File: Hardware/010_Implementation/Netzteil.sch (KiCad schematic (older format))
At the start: 6 parts, among them J1 USB_B_Mini, K1 G2R2A, U1 LT1086-3.3, U2 LM1085-3.3

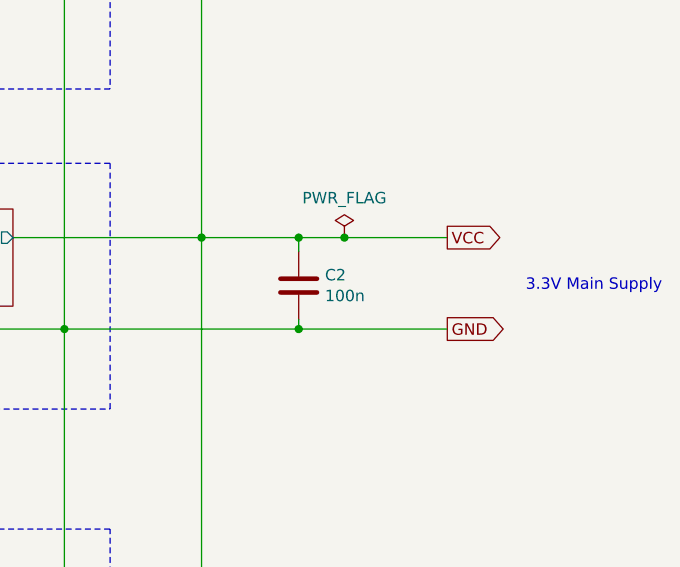
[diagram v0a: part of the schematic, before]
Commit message: Changes to Schematic. Button, LEDs and Power Flags
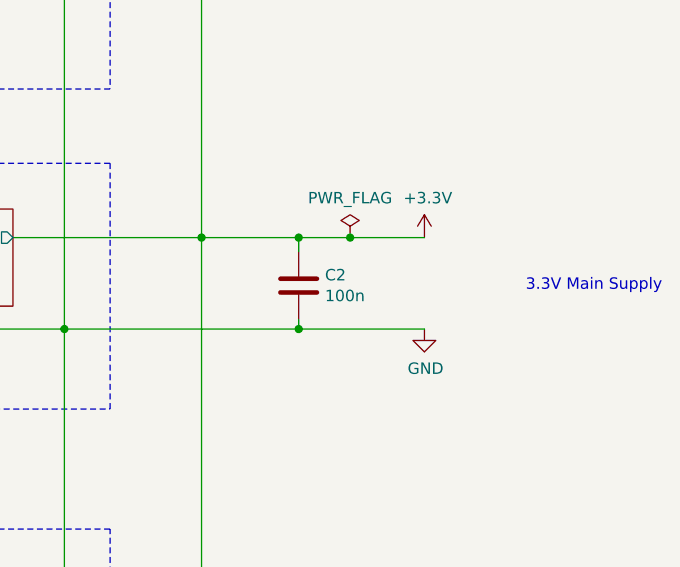
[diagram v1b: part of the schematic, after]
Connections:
- net labels added: +3.3V
- net labels removed: VCC
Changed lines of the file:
@@
 	4125 1850 3725 1850
 Connection ~ 4125 1850
-Text GLabel 9550 3450 2    50   Output ~ 0
-VCC
 Wire Wire Line
 	5725 2150 5725 2250
@@
 	8075 4725 3200 4725
 Connection ~ 6200 3450
-Text GLabel 9550 3850 2    50   Output ~ 0
-GND
 Wire Wire Line
 	8475 5325 8475 3450
@@
 F6 "V_OUT" O R 7600 5325 50
 $EndSheet
-$Comp
-L power:PWR_FLAG #FLG02
-U 1 1 5F5B0BF0
-P 9100 3450
-F 0 "#FLG02" H 9100 3525 50  0001 C CNN
-F 1 "PWR_FLAG" H 9100 3623 50  0000 C CNN
-F 2 "" H 9100 3450 50  0001 C CNN
-F 3 "~" H 9100 3450 50  0001 C CNN
-	1    9100 3450
-	1    0    0    -1
-$EndComp
-Connection ~ 9100 3450
-Wire Wire Line
-	9100 3450 9550 3450
 Wire Wire Line
 	7875 3850 8900 3850
@@
 Connection ~ 8900 3450
 Wire Wire Line
-	8900 3450 9100 3450
-Wire Wire Line
 	8900 3810 8900 3850
 Connection ~ 8900 3850
 Wire Wire Line
-	8900 3850 9550 3850
+	8900 3850 9450 3850
 Text Notes 10490 3690 2    50   ~ 0
 3.3V Main Supply
@@
 	1    0    0    -1
 $EndComp
+$Comp
+L power:GND #PWR02
+U 1 1 5F7C816E
+P 9450 3850
+F 0 "#PWR02" H 9450 3600 50  0001 C CNN
+F 1 "GND" H 9455 3677 50  0000 C CNN
+F 2 "" H 9450 3850 50  0001 C CNN
+F 3 "" H 9450 3850 50  0001 C CNN
+	1    9450 3850
+	1    0    0    -1
+$EndComp
+Wire Wire Line
+	8900 3450 9125 3450
+$Comp
+L power:+3.3V #PWR01
+U 1 1 5F7FF608
+P 9450 3450
+F 0 "#PWR01" H 9450 3300 50  0001 C CNN
+F 1 "+3.3V" H 9465 3623 50  0000 C CNN
+F 2 "" H 9450 3450 50  0001 C CNN
+F 3 "" H 9450 3450 50  0001 C CNN
+	1    9450 3450
+	1    0    0    -1
+$EndComp
+$Comp
+L power:PWR_FLAG #FLG0101
+U 1 1 5F8BED6A
+P 9125 3450
+F 0 "#FLG0101" H 9125 3525 50  0001 C CNN
+F 1 "PWR_FLAG" H 9125 3623 50  0000 C CNN
+F 2 "" H 9125 3450 50  0001 C CNN
+F 3 "~" H 9125 3450 50  0001 C CNN
+	1    9125 3450
+	1    0    0    -1
+$EndComp
+Connection ~ 9125 3450
+Wire Wire Line
+	9125 3450 9450 3450
 $EndSCHEMATC

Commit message: Updated Schematic. Fixed Connection to Ground to prevent Software Bugs
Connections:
- wire segments 54 -> 55
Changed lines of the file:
@@
 L power:PWR_FLAG #FLG01
 U 1 1 5F6C2967
-P 5250 1850
-F 0 "#FLG01" H 5250 1925 50  0001 C CNN
-F 1 "PWR_FLAG" H 5250 2023 50  0000 C CNN
-F 2 "" H 5250 1850 50  0001 C CNN
-F 3 "~" H 5250 1850 50  0001 C CNN
-	1    5250 1850
+P 5250 1775
+F 0 "#FLG01" H 5250 1850 50  0001 C CNN
+F 1 "PWR_FLAG" H 5250 1948 50  0000 C CNN
+F 2 "" H 5250 1775 50  0001 C CNN
+F 3 "~" H 5250 1775 50  0001 C CNN
+	1    5250 1775
 	1    0    0    -1
 $EndComp
@@
 Wire Wire Line
 	9125 3450 9450 3450
+Wire Wire Line
+	5250 1850 5250 1775
 $EndSCHEMATC

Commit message: Modified Board Schematic. Optimized supply and switching system through Software
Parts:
- removed C2: 100n, Capacitor_SMD:C_1812_4532Metric_Pad1.30x3.40mm_HandSolder, symbol Device:C
- removed J1: USB_B_Mini, Connector_USB:USB_Micro-B_Wuerth_629105150521_CircularHoles, symbol Connector:USB_B_Mini
- removed K1: G2R2A, Board:G2R2A, symbol Board:G2R2A
- removed U1: LT1086-3.3, Package_TO_SOT_SMD:TO-263-3_TabPin4, symbol Regulator_Linear:LT1086-3.3
- removed U2: LM1085-3.3, Package_TO_SOT_SMD:TO-263-3_TabPin4, symbol Regulator_Linear:LM1085-3.3
- added C1: 10n, Capacitor_SMD:C_1812_4532Metric_Pad1.30x3.40mm_HandSolder, symbol Device:C
- added R1: 1k, Resistor_SMD:R_0805_2012Metric_Pad1.15x1.40mm_HandSolder, symbol Device:R
- added R2: 100, Resistor_SMD:R_0805_2012Metric_Pad1.15x1.40mm_HandSolder, symbol Device:R
- added U1: LT1086-5.0, Board:DPAK254P1394X457-4N, symbol Regulator_Linear:LT1086-5.0
- renumbered C1 to C2
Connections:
- net labels added: Ext.5V, OBD_Voltage_Check
- net labels removed: +3.3V, EN_CAN, OBD_GND, USB_GND, USB_VDD
- wire segments 55 -> 22
- no-connect marks 4 -> 0
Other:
- note removed: "3.3V - MCU Power Supply"
- note removed: "3.3V Main Supply"
- note removed: "5V - External Power Supply"
- moved on the sheet: C2

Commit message: Added Missing 5V marker
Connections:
- net labels added: +5V
- net labels removed: Ext.5V
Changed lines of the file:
@@
 Wire Wire Line
 	6850 2825 7025 2825
-Text HLabel 7950 2825 2    50   Input ~ 0
-Ext.5V
 $Comp
 L power:GND #PWR02
@@
 Wire Wire Line
 	4850 4150 4650 4150
+$Comp
+L power:+5V #PWR?
+U 1 1 5FA170AE
+P 7950 2825
+F 0 "#PWR?" H 7950 2675 50  0001 C CNN
+F 1 "+5V" H 7965 2998 50  0000 C CNN
+F 2 "" H 7950 2825 50  0001 C CNN
+F 3 "" H 7950 2825 50  0001 C CNN
+	1    7950 2825
+	1    0    0    -1
+$EndComp
 $EndSCHEMATC

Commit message: Board version 4
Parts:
- removed U1: LT1086-5.0, Board:DPAK254P1394X457-4N, symbol Regulator_Linear:LT1086-5.0
- added C3: 22u, Capacitor_SMD:C_0603_1608Metric_Pad1.05x0.95mm_HandSolder, symbol Device:C
- added L1: 2.2u, Capacitor_SMD:C_0603_1608Metric_Pad1.05x0.95mm_HandSolder, symbol Device:L
- added R3: 100k, Resistor_SMD:R_0805_2012Metric_Pad1.15x1.40mm_HandSolder, symbol Device:R
- added U1: TPS62163DGK, Package_SO:VSSOP-8_3.0x3.0mm_P0.65mm, symbol Regulator_Switching:TPS62163DSG
- C1: footprint Capacitor_SMD:C_1812_4532Metric_Pad1.30x3.40mm_HandSolder -> Capacitor_SMD:C_0603_1608Metric_Pad1.05x0.95mm_HandSolder
- C2: value 100n -> 10u; footprint Capacitor_SMD:C_1812_4532Metric_Pad1.30x3.40mm_HandSolder -> Capacitor_SMD:C_0603_1608Metric_Pad1.05x0.95mm_HandSolder
- R1: value 1k -> 10k
- R2: value 100 -> 1k
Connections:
- wire segments 22 -> 44
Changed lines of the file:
@@
 Text Notes 4175 2300 2    50   ~ 0
 12V-OBD Power Supply
-Wire Wire Line
-	6850 2825 6850 2875
-Wire Wire Line
-	6850 3175 6850 3225
-$Comp
-L Device:C C2
-U 1 1 5F6089EB
-P 6850 3025
-F 0 "C2" H 6965 3071 50  0000 L CNN
-F 1 "100n" H 6965 2980 50  0000 L CNN
-F 2 "Capacitor_SMD:C_1812_4532Metric_Pad1.30x3.40mm_HandSolder" H 6888 2875 50  0001 C CNN
-F 3 "~" H 6850 3025 50  0001 C CNN
-	1    6850 3025
-	1    0    0    -1
-$EndComp
-Wire Wire Line
-	6850 2825 7025 2825
-$Comp
-L power:GND #PWR02
-U 1 1 5FA1043A
-P 7950 3300
-F 0 "#PWR02" H 7950 3050 50  0001 C CNN
-F 1 "GND" H 7955 3127 50  0000 C CNN
-F 2 "" H 7950 3300 50  0001 C CNN
-F 3 "" H 7950 3300 50  0001 C CNN
-	1    7950 3300
-	1    0    0    -1
-$EndComp
-Wire Wire Line
-	7950 3225 7950 3300
-Wire Wire Line
-	6850 2825 6775 2825
-Connection ~ 6850 2825
-Wire Wire Line
-	7625 2825 7950 2825
-$Comp
-L Regulator_Linear:LT1086-5.0 U1
-U 1 1 5FA0C017
-P 7325 2825
-F 0 "U1" H 7325 3067 50  0000 C CNN
-F 1 "LT1086-5.0" H 7325 2976 50  0000 C CNN
-F 2 "Board:DPAK254P1394X457-4N" H 7325 3075 50  0001 C CIN
-F 3 "https://www.analog.com/media/en/technical-documentation/data-sheets/1086ffs.pdf" H 7325 2825 50  0001 C CNN
-	1    7325 2825
-	1    0    0    -1
-$EndComp
-Wire Wire Line
-	6850 3225 7325 3225
-Wire Wire Line
-	7325 3125 7325 3225
-Connection ~ 7325 3225
-Wire Wire Line
-	7325 3225 7950 3225
 $Comp
 L Device:R R1
@@
 P 5025 3425
 F 0 "R1" H 5095 3471 50  0000 L CNN
-F 1 "1k" H 5095 3380 50  0000 L CNN
+F 1 "10k" H 5095 3380 50  0000 L CNN
 F 2 "Resistor_SMD:R_0805_2012Metric_Pad1.15x1.40mm_HandSolder" V 4955 3425 50  0001 C CNN
 F 3 "~" H 5025 3425 50  0001 C CNN
@@
 P 5025 3875
 F 0 "R2" H 5095 3921 50  0000 L CNN
-F 1 "100" H 5095 3830 50  0000 L CNN
+F 1 "1k" H 5095 3830 50  0000 L CNN
 F 2 "Resistor_SMD:R_0805_2012Metric_Pad1.15x1.40mm_HandSolder" V 4955 3875 50  0001 C CNN
 F 3 "~" H 5025 3875 50  0001 C CNN
@@
 L power:PWR_FLAG #FLG01
 U 1 1 5FB093DE
-P 6775 2825
-F 0 "#FLG01" H 6775 2900 50  0001 C CNN
-F 1 "PWR_FLAG" H 6775 2998 50  0000 C CNN
-F 2 "" H 6775 2825 50  0001 C CNN
-F 3 "~" H 6775 2825 50  0001 C CNN
-	1    6775 2825
-	1    0    0    -1
-$EndComp
-Connection ~ 6775 2825
-Wire Wire Line
-	6775 2825 5025 2825
+P 5425 2825
+F 0 "#FLG01" H 5425 2900 50  0001 C CNN
+F 1 "PWR_FLAG" H 5425 2998 50  0000 C CNN
+F 2 "" H 5425 2825 50  0001 C CNN
+F 3 "~" H 5425 2825 50  0001 C CNN
+	1    5425 2825
+	1    0    0    -1
+$EndComp
 $Comp
 L Device:C C1
@@
 F 0 "C1" H 4765 3921 50  0000 L CNN
 F 1 "10n" H 4765 3830 50  0000 L CNN
-F 2 "Capacitor_SMD:C_1812_4532Metric_Pad1.30x3.40mm_HandSolder" H 4688 3725 50  0001 C CNN
+F 2 "Capacitor_SMD:C_0603_1608Metric_Pad1.05x0.95mm_HandSolder" H 4688 3725 50  0001 C CNN
 F 3 "~" H 4650 3875 50  0001 C CNN
 	1    4650 3875
@@
 	4850 4150 4650 4150
 $Comp
-L power:+5V #PWR021
+L power:+5V #PWR05
 U 1 1 5FA170AE
-P 7950 2825
-F 0 "#PWR021" H 7950 2675 50  0001 C CNN
-F 1 "+5V" H 7965 2998 50  0000 C CNN
-F 2 "" H 7950 2825 50  0001 C CNN
-F 3 "" H 7950 2825 50  0001 C CNN
-	1    7950 2825
-	1    0    0    -1
-$EndComp
+P 10625 2750
+F 0 "#PWR05" H 10625 2600 50  0001 C CNN
+F 1 "+5V" H 10640 2923 50  0000 C CNN
+F 2 "" H 10625 2750 50  0001 C CNN
+F 3 "" H 10625 2750 50  0001 C CNN
+	1    10625 2750
+	1    0    0    -1
+$EndComp
+Connection ~ 5425 2825
+Wire Wire Line
+	5425 2825 5025 2825
+Wire Wire Line
+	5425 2825 6975 2825
+$Comp
+L Regulator_Switching:TPS62163DSG U1
+U 1 1 5FB37DEF
+P 7975 3125
+F 0 "U1" H 7975 3692 50  0000 C CNN
+F 1 "TPS62163DGK" H 7975 3601 50  0000 C CNN
+F 2 "Package_SO:VSSOP-8_3.0x3.0mm_P0.65mm" H 8125 2775 50  0001 L CNN
+F 3 "http://www.ti.com/lit/ds/symlink/tps62160.pdf" H 7975 3675 50  0001 C CNN
+	1    7975 3125
+	1    0    0    -1
+$EndComp
+$Comp
+L Device:L L1
+U 1 1 5FB3AA0A
+P 8650 2825
+F 0 "L1" V 8840 2825 50  0000 C CNN
+F 1 "2.2u" V 8749 2825 50  0000 C CNN
+F 2 "Capacitor_SMD:C_0603_1608Metric_Pad1.05x0.95mm_HandSolder" H 8650 2825 50  0001 C CNN
+F 3 "~" H 8650 2825 50  0001 C CNN
+	1    8650 2825
+	0    -1   -1   0
+$EndComp
+$Comp
+L Device:R R3
+U 1 1 5FB3B31A
+P 8250 4225
+F 0 "R3" V 8043 4225 50  0000 C CNN
+F 1 "100k" V 8134 4225 50  0000 C CNN
+F 2 "Resistor_SMD:R_0805_2012Metric_Pad1.15x1.40mm_HandSolder" V 8180 4225 50  0001 C CNN
+F 3 "~" H 8250 4225 50  0001 C CNN
+	1    8250 4225
+	0    1    1    0
+$EndComp
+Wire Wire Line
+	8375 2825 8500 2825
+Wire Wire Line
+	8800 2825 8925 2825
+Wire Wire Line
+	7575 3225 7575 4225
+Wire Wire Line
+	7575 4225 8100 4225
+Wire Wire Line
+	8925 4225 8925 2925
+Connection ~ 8925 2825
+Wire Wire Line
+	8400 4225 8925 4225
+$Comp
+L power:GND #PWR03
+U 1 1 5FB3F4B3
+P 7975 3750
+F 0 "#PWR03" H 7975 3500 50  0001 C CNN
+F 1 "GND" H 7980 3577 50  0000 C CNN
+F 2 "" H 7975 3750 50  0001 C CNN
+F 3 "" H 7975 3750 50  0001 C CNN
+	1    7975 3750
+	1    0    0    -1
+$EndComp
+Wire Wire Line
+	7975 3750 7975 3575
+Wire Wire Line
+	8075 3575 8075 3525
+Connection ~ 7975 3575
+Wire Wire Line
+	7975 3575 8075 3575
+Wire Wire Line
+	7975 3525 7975 3575
+Wire Wire Line
+	8375 2925 8925 2925
+Connection ~ 8925 2925
+Wire Wire Line
+	8925 2925 8925 2825
+$Comp
+L Device:C C2
+U 1 1 5FB43F56
+P 6975 3100
+F 0 "C2" H 7090 3146 50  0000 L CNN
+F 1 "10u" H 7090 3055 50  0000 L CNN
+F 2 "Capacitor_SMD:C_0603_1608Metric_Pad1.05x0.95mm_HandSolder" H 7013 2950 50  0001 C CNN
+F 3 "~" H 6975 3100 50  0001 C CNN
+	1    6975 3100
+	1    0    0    -1
+$EndComp
+Wire Wire Line
+	7575 2925 7450 2925
+Wire Wire Line
+	7450 2925 7450 2825
+Connection ~ 7450 2825
+Wire Wire Line
+	7450 2825 7575 2825
+Wire Wire Line
+	6975 2950 6975 2825
+Connection ~ 6975 2825
+Wire Wire Line
+	6975 2825 7450 2825
+$Comp
+L power:GND #PWR02
+U 1 1 5FB459AA
+P 6975 3425
+F 0 "#PWR02" H 6975 3175 50  0001 C CNN
+F 1 "GND" H 6980 3252 50  0000 C CNN
+F 2 "" H 6975 3425 50  0001 C CNN
+F 3 "" H 6975 3425 50  0001 C CNN
+	1    6975 3425
+	1    0    0    -1
+$EndComp
+Wire Wire Line
+	6975 3425 6975 3250
+$Comp
+L power:GND #PWR04
+U 1 1 5FB4620B
+P 9975 3500
+F 0 "#PWR04" H 9975 3250 50  0001 C CNN
+F 1 "GND" H 9980 3327 50  0000 C CNN
+F 2 "" H 9975 3500 50  0001 C CNN
+F 3 "" H 9975 3500 50  0001 C CNN
+	1    9975 3500
+	1    0    0    -1
+$EndComp
+Wire Wire Line
+	10625 2825 10625 2750
+$Comp
+L Device:C C3
+U 1 1 5FB437F9
+P 9975 3025
+F 0 "C3" H 10090 3071 50  0000 L CNN
+F 1 "22u" H 10090 2980 50  0000 L CNN
+F 2 "Capacitor_SMD:C_0603_1608Metric_Pad1.05x0.95mm_HandSolder" H 10013 2875 50  0001 C CNN
+F 3 "~" H 9975 3025 50  0001 C CNN
+	1    9975 3025
+	1    0    0    -1
+$EndComp
+Wire Wire Line
+	8925 2825 9975 2825
+Wire Wire Line
+	9975 2875 9975 2825
+Connection ~ 9975 2825
+Wire Wire Line
+	9975 2825 10450 2825
+Wire Wire Line
+	9975 3275 9525 3275
+Wire Wire Line
+	9525 3275 9525 3025
+Wire Wire Line
+	9525 3025 8375 3025
+Wire Wire Line
+	9975 3175 9975 3275
+Wire Wire Line
+	9975 3275 9975 3500
+Connection ~ 9975 3275
+$Comp
+L power:PWR_FLAG #FLG02
+U 1 1 5FB4D740
+P 10450 2825
+F 0 "#FLG02" H 10450 2900 50  0001 C CNN
+F 1 "PWR_FLAG" H 10450 2998 50  0000 C CNN
+F 2 "" H 10450 2825 50  0001 C CNN
+F 3 "~" H 10450 2825 50  0001 C CNN
+	1    10450 2825
+	1    0    0    -1
+$EndComp
+Connection ~ 10450 2825
+Wire Wire Line
+	10450 2825 10625 2825
+Wire Wire Line
+	7875 3525 7875 3575
+Wire Wire Line
+	7875 3575 7975 3575
 $EndSCHEMATC

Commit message: Board Version 4.2
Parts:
- added C10: C, symbol Device:C
- added C16: 10u, symbol Device:C
- added C9: 100n, Capacitor_SMD:C_0603_1608Metric_Pad1.05x0.95mm_HandSolder, symbol Device:C
- added D8: D, symbol Device:D
- added F1: Fuse, symbol Device:Fuse
- added FB1, FB2: Ferrite_Bead, symbol Device:Ferrite_Bead
- added L3: 5u, symbol Device:L_Core_Iron
- added R19: 953k, symbol Device:R
- added R20: 180k, symbol Device:R
- R3: value 100k -> 10k
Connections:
- net +5V: now also C10.1, FB2.1; no longer C3.1, L1.2, R3.1, U1.6 (VOS)
- net GND: now also C10.2, C16.2, C9.2, D8.2 (A), R20.2; no longer U1.5 (FB)
- net OBD_VDD: now also F1.2; no longer C2.1, R1.1, U1.2 (VIN), U1.3 (EN)
- new net: C3.1, FB2.2, L1.2, R19.1, R3.1, U1.6 (VOS)
- new net: R19.2, R20.1, U1.5 (FB)
- new net: C16.1, C9.1, FB1.2, L3.1, R1.1
- new net: C2.1, FB1.1, U1.2 (VIN), U1.3 (EN)
- new net: D8.1 (K), F1.1, L3.2
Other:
- moved on the sheet: C1, C2, C3, L1, R1, R2, R3, U1
